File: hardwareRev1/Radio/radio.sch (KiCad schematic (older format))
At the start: 27 parts, among them J1 SMA, U1 AX503, U2 PE42424, X1 TCXO

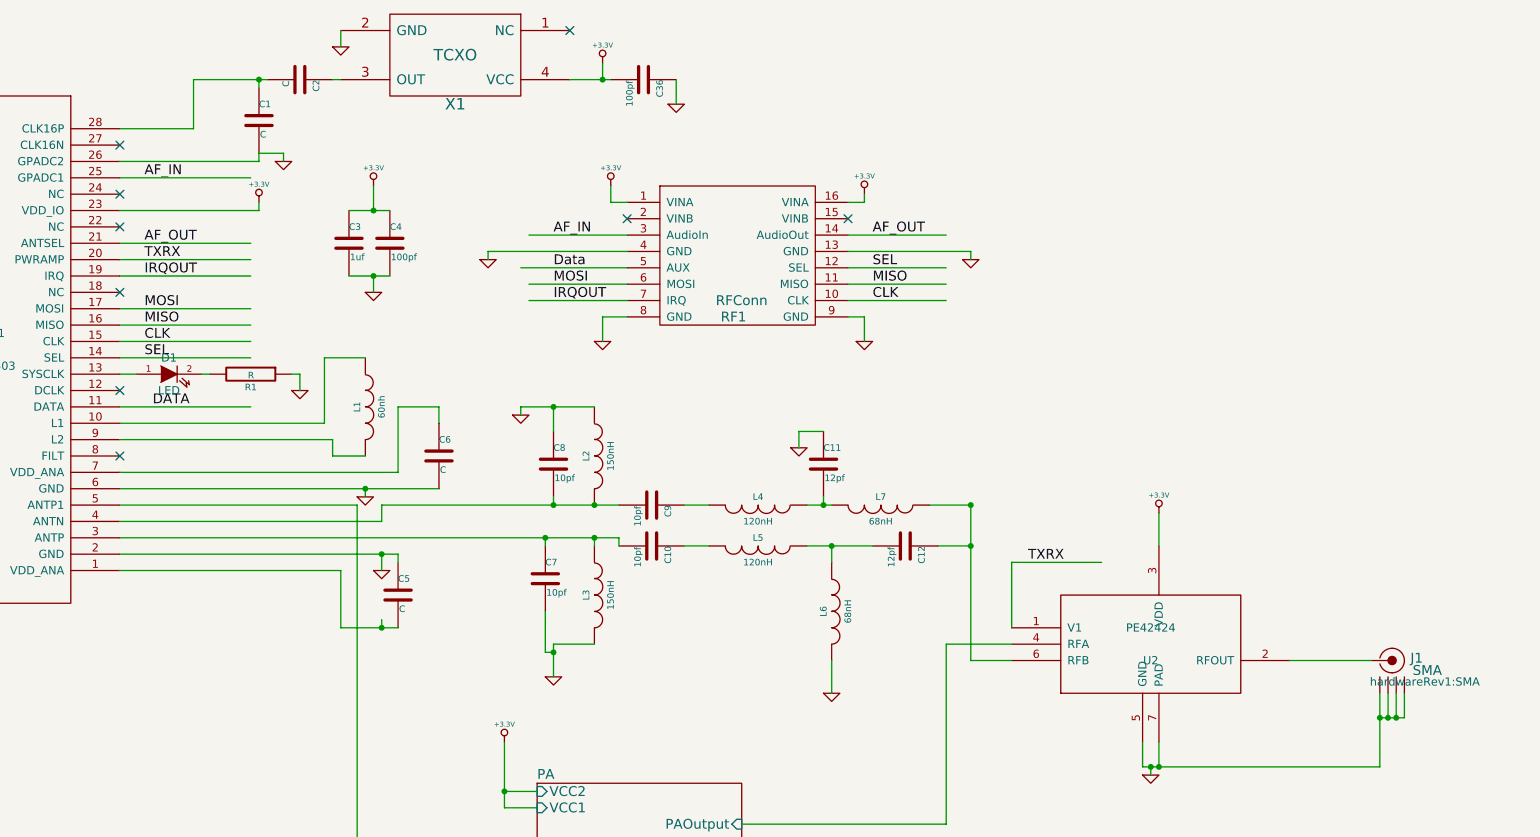
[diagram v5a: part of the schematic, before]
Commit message: Finished the new radio module schematic.
Added a MCU beacause having 4 layers is an auful waste of space.
Added a GPS
Added an edge mount SMA component.
Added the NEO-7 hardware integration manual.
Need to finish the schematic.
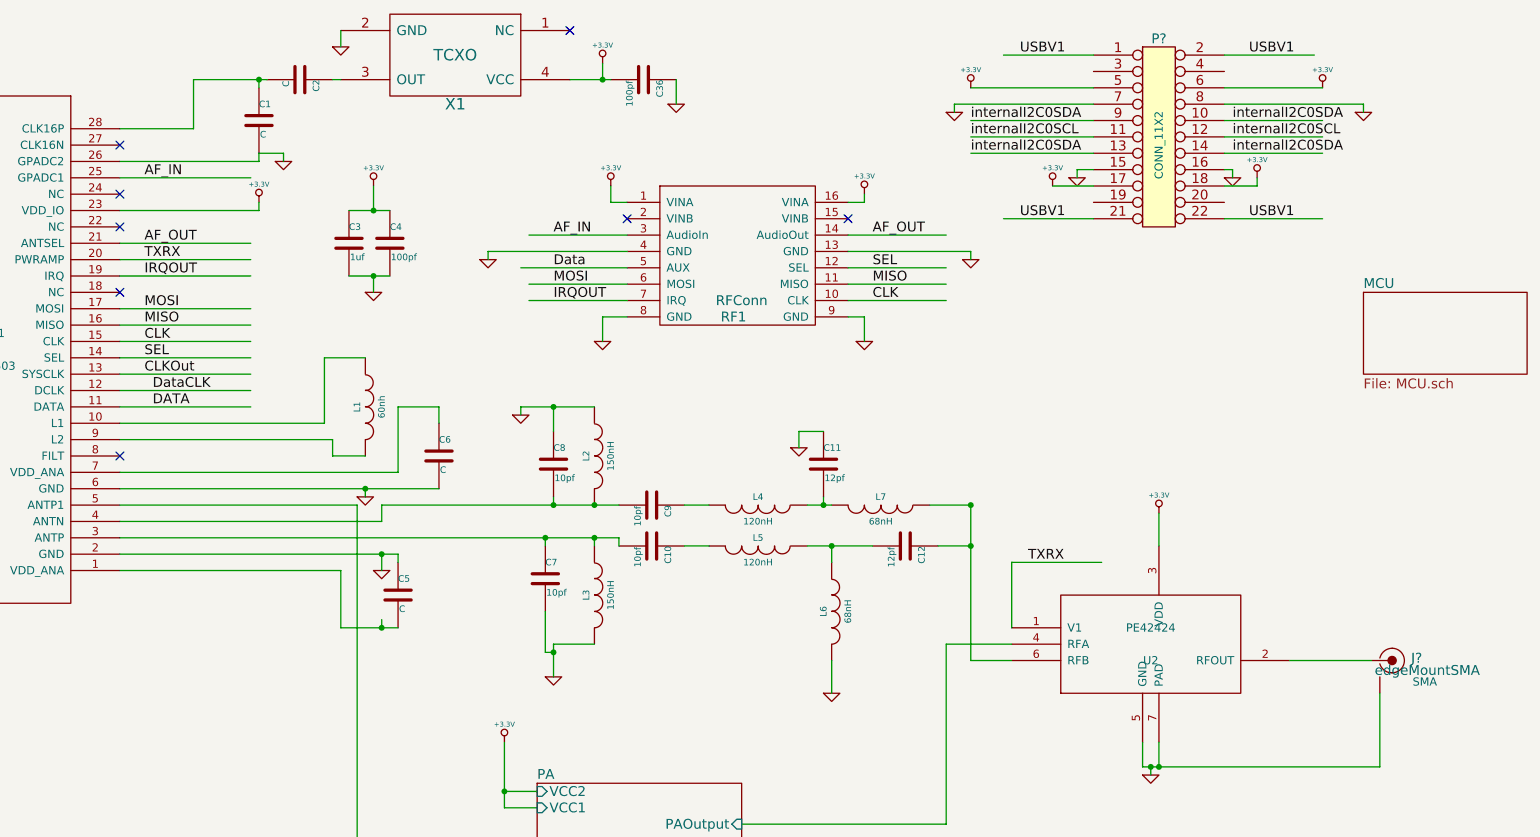
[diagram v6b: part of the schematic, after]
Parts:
- removed D1: LED, LEDs:LED-0603, symbol LED
- removed J1: SMA, hardwareRev1:SMA, symbol SMA
- removed R1: R, Resistors_SMD:R_0402, symbol R
- added J?: edgeMountSMA, SMA, symbol edgeMountSMA
- added P?: CONN_11X2, symbol CONN_11X2
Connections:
- net labels added: CLKOut, DataCLK, USBV1, internalI2C0SCL, internalI2C0SDA
- wire segments 122 -> 139
- no-connect marks 9 -> 8
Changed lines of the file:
@@
 LIBS:RFConn
 LIBS:sma
+LIBS:conn_11x2
+LIBS:SparkFun
+LIBS:smtJmpOpen
+LIBS:neo7
+LIBS:MKL26Z128VLH4
+LIBS:USB
+LIBS:open-project
 LIBS:radio-cache
 EELAYER 25 0
@@
 $Descr A4 11693 8268
 encoding utf-8
-Sheet 1 2
+Sheet 1 3
 Title ""
 Date ""
@@
 	3250 3950 3250 3850
 Connection ~ 3250 3850
-$Comp
-L SMA J1
-U 1 1 55EDAF09
-P 9450 4800
-F 0 "J1" H 9575 5115 60  0000 C CNN
-F 1 "SMA" H 9640 5040 60  0000 C CNN
-F 2 "hardwareRev1:SMA" H 9625 4970 50  0000 C CNN
-F 3 "" H 9450 4800 60  0000 C CNN
-	1    9450 4800
-	1    0    0    -1
-$EndComp
-Wire Wire Line
-	9500 4700 9500 4850
-Wire Wire Line
-	9500 4850 9350 4850
-Wire Wire Line
-	9350 5150 9350 4700
-Wire Wire Line
-	9400 4700 9400 4850
-Connection ~ 9400 4850
-Wire Wire Line
-	9450 4700 9450 4850
-Connection ~ 9450 4850
 Connection ~ 8000 5150
-Connection ~ 9350 4850
 $Comp
 L RFConn RF1
@@
 NoConn ~ 1650 1850
 NoConn ~ 1650 2250
-$Comp
-L LED D1
-U 1 1 55EDC42A
-P 1950 2750
-F 0 "D1" H 1950 2850 50  0000 C CNN
-F 1 "LED" H 1950 2650 50  0000 C CNN
-F 2 "LEDs:LED-0603" H 1950 2750 60  0001 C CNN
-F 3 "" H 1950 2750 60  0000 C CNN
-	1    1950 2750
-	1    0    0    -1
-$EndComp
-$Comp
-L R R1
-U 1 1 55EDC4AC
-P 2450 2750
-F 0 "R1" V 2530 2750 40  0000 C CNN
-F 1 "R" V 2457 2751 40  0000 C CNN
-F 2 "Resistors_SMD:R_0402" V 2380 2750 30  0001 C CNN
-F 3 "" H 2450 2750 30  0000 C CNN
-	1    2450 2750
-	0    1    1    0
-$EndComp
-$Comp
-L GND #PWR4
-U 1 1 55EDC519
-P 2750 2850
-F 0 "#PWR4" H 2750 2850 30  0001 C CNN
-F 1 "GND" H 2750 2780 30  0001 C CNN
-F 2 "" H 2750 2850 60  0000 C CNN
-F 3 "" H 2750 2850 60  0000 C CNN
-	1    2750 2850
-	1    0    0    -1
-$EndComp
 Wire Wire Line
 	1650 1950 2450 1950
 NoConn ~ 1650 3250
-NoConn ~ 1650 2850
 Text Label 1800 1950 0    60   ~ 0
 AF_OUT
 Wire Wire Line
-	1650 2750 1750 2750
-Wire Wire Line
-	2150 2750 2200 2750
-Wire Wire Line
-	2700 2750 2750 2750
-Wire Wire Line
-	2750 2750 2750 2850
+	1650 2750 2450 2750
 Wire Wire Line
 	6100 1900 6700 1900
@@
 Wire Wire Line
 	4100 2100 4750 2100
+$Comp
+L CONN_11X2 P?
+U 1 1 55F493DB
+P 8000 1250
+F 0 "P?" H 8000 1800 60  0000 C CNN
+F 1 "CONN_11X2" V 8000 1150 50  0000 C CNN
+F 2 "" H 8000 1250 60  0000 C CNN
+F 3 "" H 8000 1250 60  0000 C CNN
+	1    8000 1250
+	1    0    0    -1
+$EndComp
+Wire Wire Line
+	7600 1000 6850 1000
+Wire Wire Line
+	8400 1000 9000 1000
+Wire Wire Line
+	8400 1100 9250 1100
+Wire Wire Line
+	6750 1100 7600 1100
+Wire Wire Line
+	7600 1200 6850 1200
+Wire Wire Line
+	7600 1300 6850 1300
+Wire Wire Line
+	8400 1200 9000 1200
+Wire Wire Line
+	8400 1300 9000 1300
+Wire Wire Line
+	8400 1400 9000 1400
+$Comp
+L +3.3V #PWR?
+U 1 1 55F4A7BA
+P 6850 1000
+F 0 "#PWR?" H 6850 960 30  0001 C CNN
+F 1 "+3.3V" H 6850 1110 30  0000 C CNN
+F 2 "" H 6850 1000 60  0000 C CNN
+F 3 "" H 6850 1000 60  0000 C CNN
+	1    6850 1000
+	1    0    0    -1
+$EndComp
+$Comp
+L +3.3V #PWR?
+U 1 1 55F4A7F6
+P 9000 1000
+F 0 "#PWR?" H 9000 960 30  0001 C CNN
+F 1 "+3.3V" H 9000 1110 30  0000 C CNN
+F 2 "" H 9000 1000 60  0000 C CNN
+F 3 "" H 9000 1000 60  0000 C CNN
+	1    9000 1000
+	1    0    0    -1
+$EndComp
+$Comp
+L GND #PWR?
+U 1 1 55F4A832
+P 6750 1150
+F 0 "#PWR?" H 6750 1150 30  0001 C CNN
+F 1 "GND" H 6750 1080 30  0001 C CNN
+F 2 "" H 6750 1150 60  0000 C CNN
+F 3 "" H 6750 1150 60  0000 C CNN
+	1    6750 1150
+	1    0    0    -1
+$EndComp
+$Comp
+L GND #PWR?
+U 1 1 55F4A8BE
+P 9250 1150
+F 0 "#PWR?" H 9250 1150 30  0001 C CNN
+F 1 "GND" H 9250 1080 30  0001 C CNN
+F 2 "" H 9250 1150 60  0000 C CNN
+F 3 "" H 9250 1150 60  0000 C CNN
+	1    9250 1150
+	1    0    0    -1
+$EndComp
+Text Label 6850 1200 0    60   ~ 0
+internalI2C0SDA
+Text Label 6850 1300 0    60   ~ 0
+internalI2C0SCL
+$Comp
+L GND #PWR?
+U 1 1 55F4A9C4
+P 7500 1550
+F 0 "#PWR?" H 7500 1550 30  0001 C CNN
+F 1 "GND" H 7500 1480 30  0001 C CNN
+F 2 "" H 7500 1550 60  0000 C CNN
+F 3 "" H 7500 1550 60  0000 C CNN
+	1    7500 1550
+	1    0    0    -1
+$EndComp
+$Comp
+L +3.3V #PWR?
+U 1 1 55F4AA9E
+P 7350 1600
+F 0 "#PWR?" H 7350 1560 30  0001 C CNN
+F 1 "+3.3V" H 7350 1710 30  0000 C CNN
+F 2 "" H 7350 1600 60  0000 C CNN
+F 3 "" H 7350 1600 60  0000 C CNN
+	1    7350 1600
+	1    0    0    -1
+$EndComp
+Wire Wire Line
+	7600 1400 6850 1400
+Text Label 6850 1400 0    60   ~ 0
+internalI2C0SDA
+Text Label 8450 1200 0    60   ~ 0
+internalI2C0SDA
+Text Label 8450 1300 0    60   ~ 0
+internalI2C0SCL
+Text Label 8450 1400 0    60   ~ 0
+internalI2C0SDA
+Wire Wire Line
+	9250 1100 9250 1150
+Wire Wire Line
+	6750 1100 6750 1150
+Wire Wire Line
+	7600 1500 7500 1500
+Wire Wire Line
+	7500 1500 7500 1550
+Wire Wire Line
+	7350 1600 7600 1600
+$Comp
+L GND #PWR?
+U 1 1 55F4B33E
+P 8450 1550
+F 0 "#PWR?" H 8450 1550 30  0001 C CNN
+F 1 "GND" H 8450 1480 30  0001 C CNN
+F 2 "" H 8450 1550 60  0000 C CNN
+F 3 "" H 8450 1550 60  0000 C CNN
+	1    8450 1550
+	1    0    0    -1
+$EndComp
+$Comp
+L +3.3V #PWR?
+U 1 1 55F4B37A
+P 8600 1550
+F 0 "#PWR?" H 8600 1510 30  0001 C CNN
+F 1 "+3.3V" H 8600 1660 30  0000 C CNN
+F 2 "" H 8600 1550 60  0000 C CNN
+F 3 "" H 8600 1550 60  0000 C CNN
+	1    8600 1550
+	1    0    0    -1
+$EndComp
+Wire Wire Line
+	8400 1500 8450 1500
+Wire Wire Line
+	8450 1500 8450 1550
+Wire Wire Line
+	8400 1600 8600 1600
+Wire Wire Line
+	8600 1600 8600 1550
+$Comp
+L edgeMountSMA J?
+U 1 1 55F4B7AB
+P 9450 4800
+F 0 "J?" H 9575 5115 60  0000 C CNN
+F 1 "edgeMountSMA" H 9640 5040 60  0000 C CNN
+F 2 "SMA" H 9625 4970 50  0000 C CNN
+F 3 "" H 9450 4800 60  0000 C CNN
+	1    9450 4800
+	1    0    0    -1
+$EndComp
+Wire Wire Line
+	9350 5150 9350 4700
+$Sheet
+S 9250 2250 1000 500
+U 55F4BACA
+F0 "MCU" 60
+F1 "MCU.sch" 60
+$EndSheet
+Text Label 1800 2750 0    60   ~ 0
+CLKOut
+Text Label 1850 2850 0    60   ~ 0
+DataCLK
+Wire Wire Line
+	1650 2850 2450 2850
+Wire Wire Line
+	8400 800  8950 800
+Wire Wire Line
+	7600 800  7050 800
+Wire Wire Line
+	8400 1800 9000 1800
+Wire Wire Line
+	7600 1800 7050 1800
+Text Label 8550 1800 0    60   ~ 0
+USBV1
+Text Label 8550 800  0    60   ~ 0
+USBV1
+Text Label 7150 800  0    60   ~ 0
+USBV1
+Text Label 7150 1800 0    60   ~ 0
+USBV1
 $EndSCHEMATC

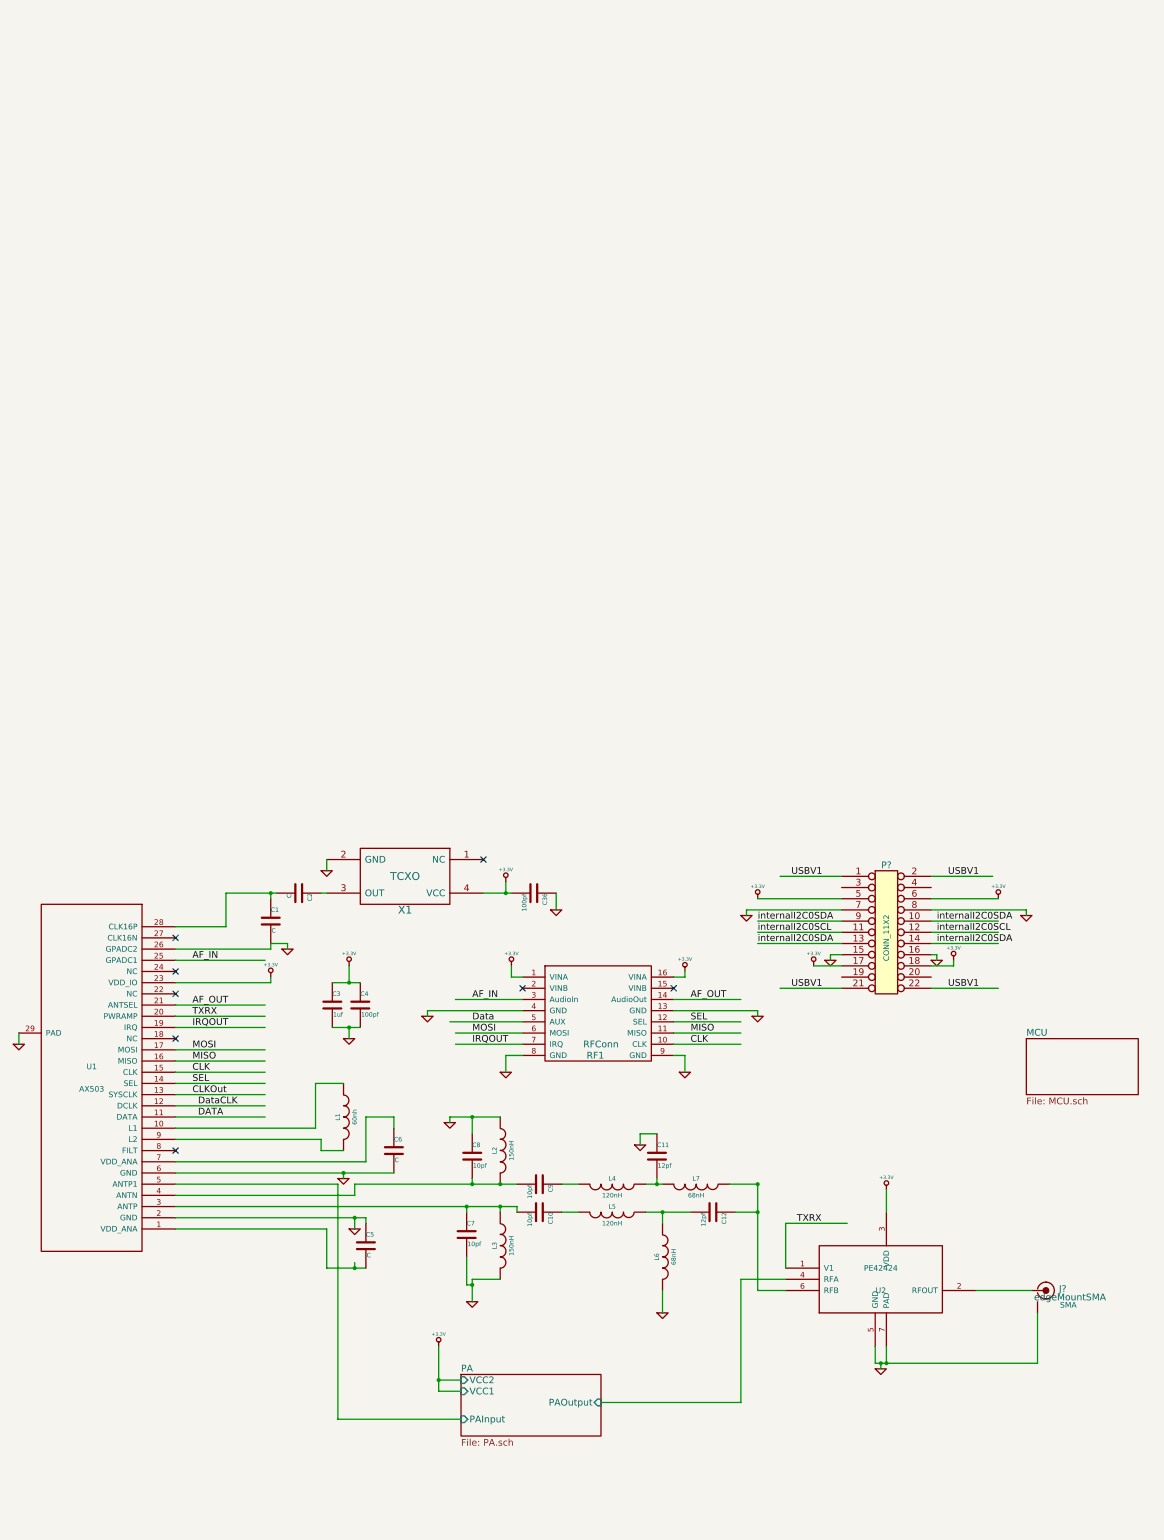
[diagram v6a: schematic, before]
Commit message: Made the board 4 layer.
Added a MCU to theback...
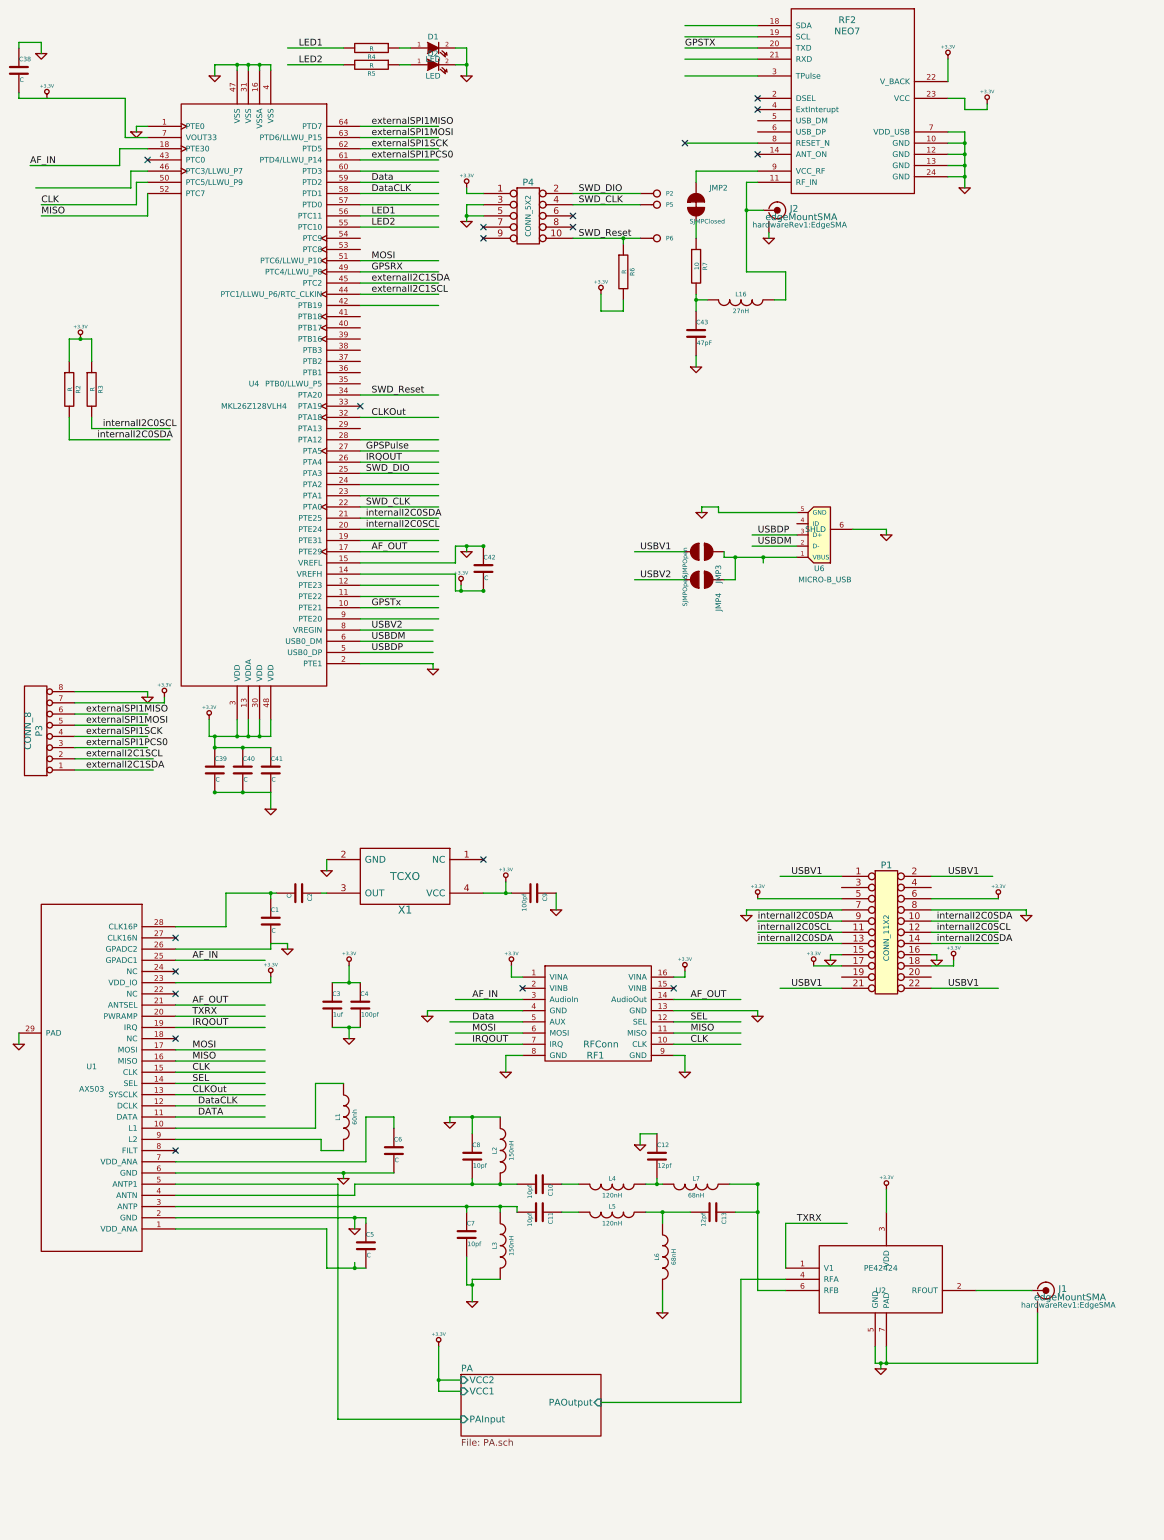
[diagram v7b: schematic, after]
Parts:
- added C38, C39, C40, C41, C42: C, Capacitors_SMD:C_0402, symbol C
- added C43: 47pF, Capacitors_SMD:C_0402, symbol C
- added D1, D2: LED, LEDs:LED-0603, symbol LED
- added J2: edgeMountSMA, hardwareRev1:EdgeSMA, symbol edgeMountSMA
- added JMP2: SJMPClosed, hardwareRev1:SMDJMP-CLOSED, symbol SJMPClosed
- added JMP3, JMP4: SJMPOpen, hardwareRev1:SMDJMP-OPEN, symbol SJMPOpen
- added L16: 27nH, Resistors_SMD:R_0402, symbol INDUCTOR
- added P2, P5, P6: CONN_1, Measurement_Points:Measurement_Point_Round-SMD-Pad_Small, symbol CONN_1
- added P3: CONN_8, Connectors_Molex:Connector_Molex_PicoBlade_53398-0871, symbol CONN_8
- added P4: CONN_5X2, hardwareRev1:CortexDebug, symbol CONN_5X2
- added R2, R3, R4, R5, R6: R, Resistors_SMD:R_0402, symbol R
- added R7: 10, Resistors_SMD:R_0402, symbol R
- added RF2: NEO7, hardwareRev1:NEO-7, symbol NEO7
- added U4: MKL26Z128VLH4, w_smd_lqfp:lqfp64, symbol MKL26Z128VLH4
- added U6: MICRO-B_USB, USB:USB micro-female, symbol MICRO-B_USB
- J1: renamed from J?; footprint SMA -> hardwareRev1:EdgeSMA
- P1: renamed from P?; footprint (none) -> hardwareRev1:1.27mmPitchHeader11X2
- renumbered C9 to C10, C10 to C11, C11 to C12, C12 to C13, C36 to C9
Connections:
- net labels added: GPSPulse, GPSRX, GPSTX, GPSTx, LED1, LED2, SWD_CLK, SWD_DIO, SWD_Reset, USBDM, USBDP, USBV2, externalI2C1SCL, externalI2C1SDA, externalSPI1MISO, externalSPI1MOSI, externalSPI1PCS0, externalSPI1SCK
- wire segments 139 -> 301
- no-connect marks 8 -> 18
